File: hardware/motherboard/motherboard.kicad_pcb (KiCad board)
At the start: 2 copper layers, 220 x 150 mm, 14 parts, among them J1 01x02_Screw_ECG, J2 01x02_Screw_5VDC_IN, J3 RCA_L_Female_Tweeter, J4 RCA_R_Female_Sub, U1 DSP-MODULE_IDC_J3, U2 MCU-MODULE, U3 ECG-MODULE, U4 DSP-MODULE_IDC_J4, U5 PROTO-MODULE, U6 DSP-MODULE_RCA_J3

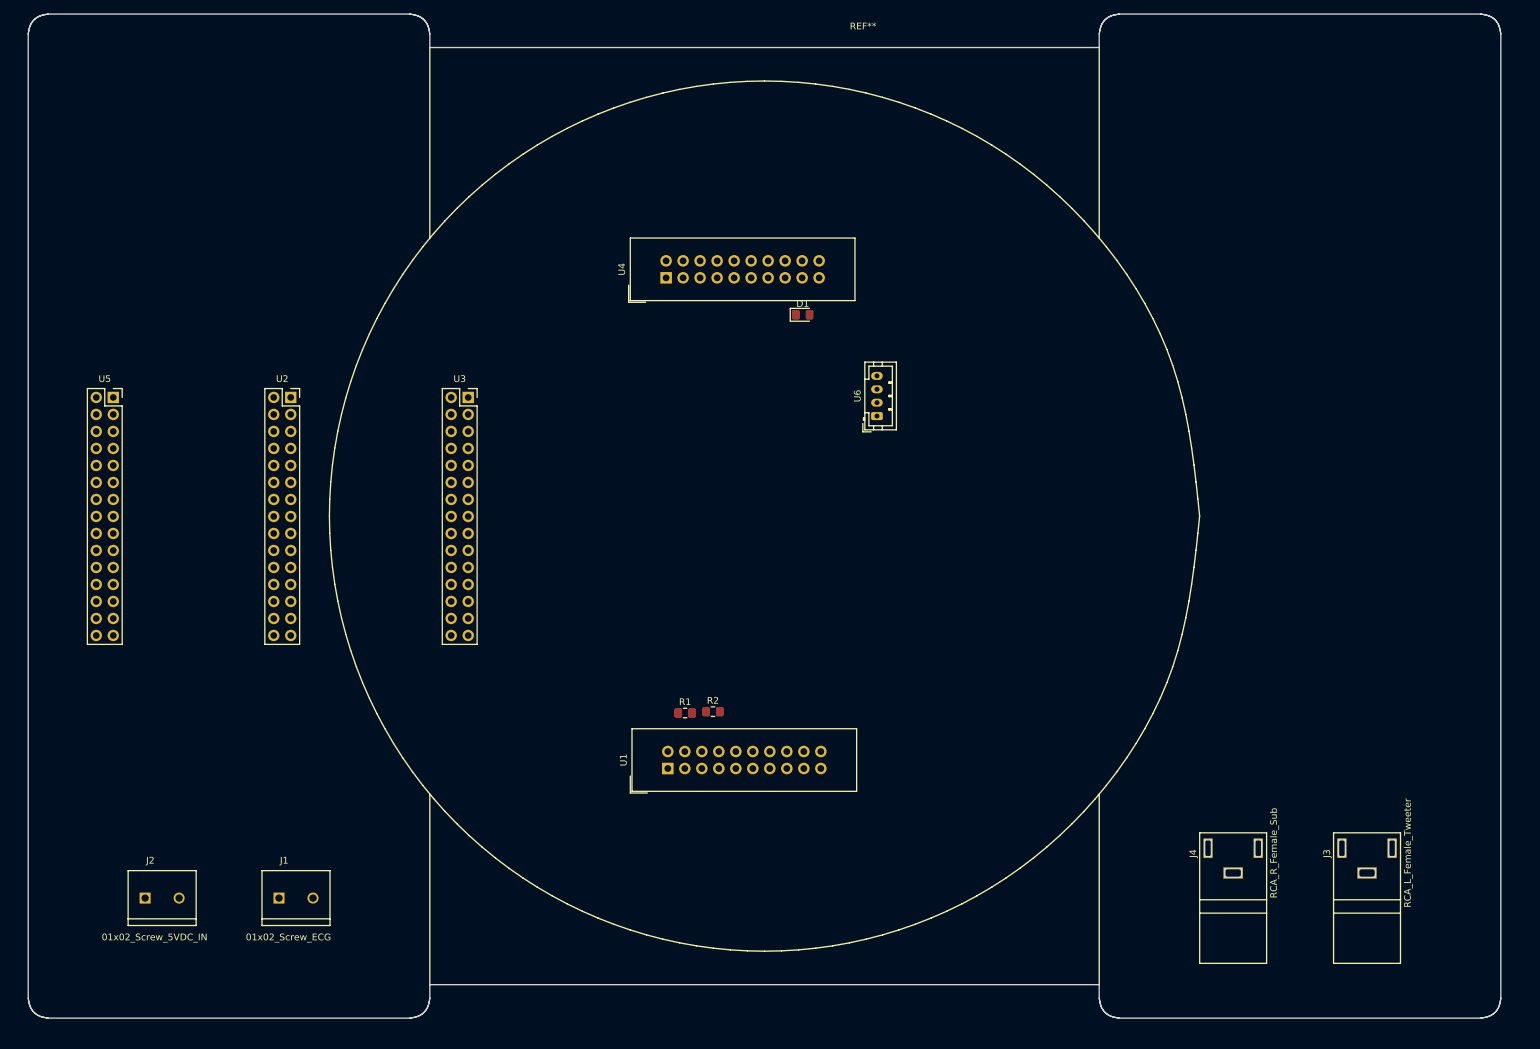
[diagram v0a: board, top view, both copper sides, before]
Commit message: [hw] Add jumper, pwr led, silkscreen logo to Motherboard
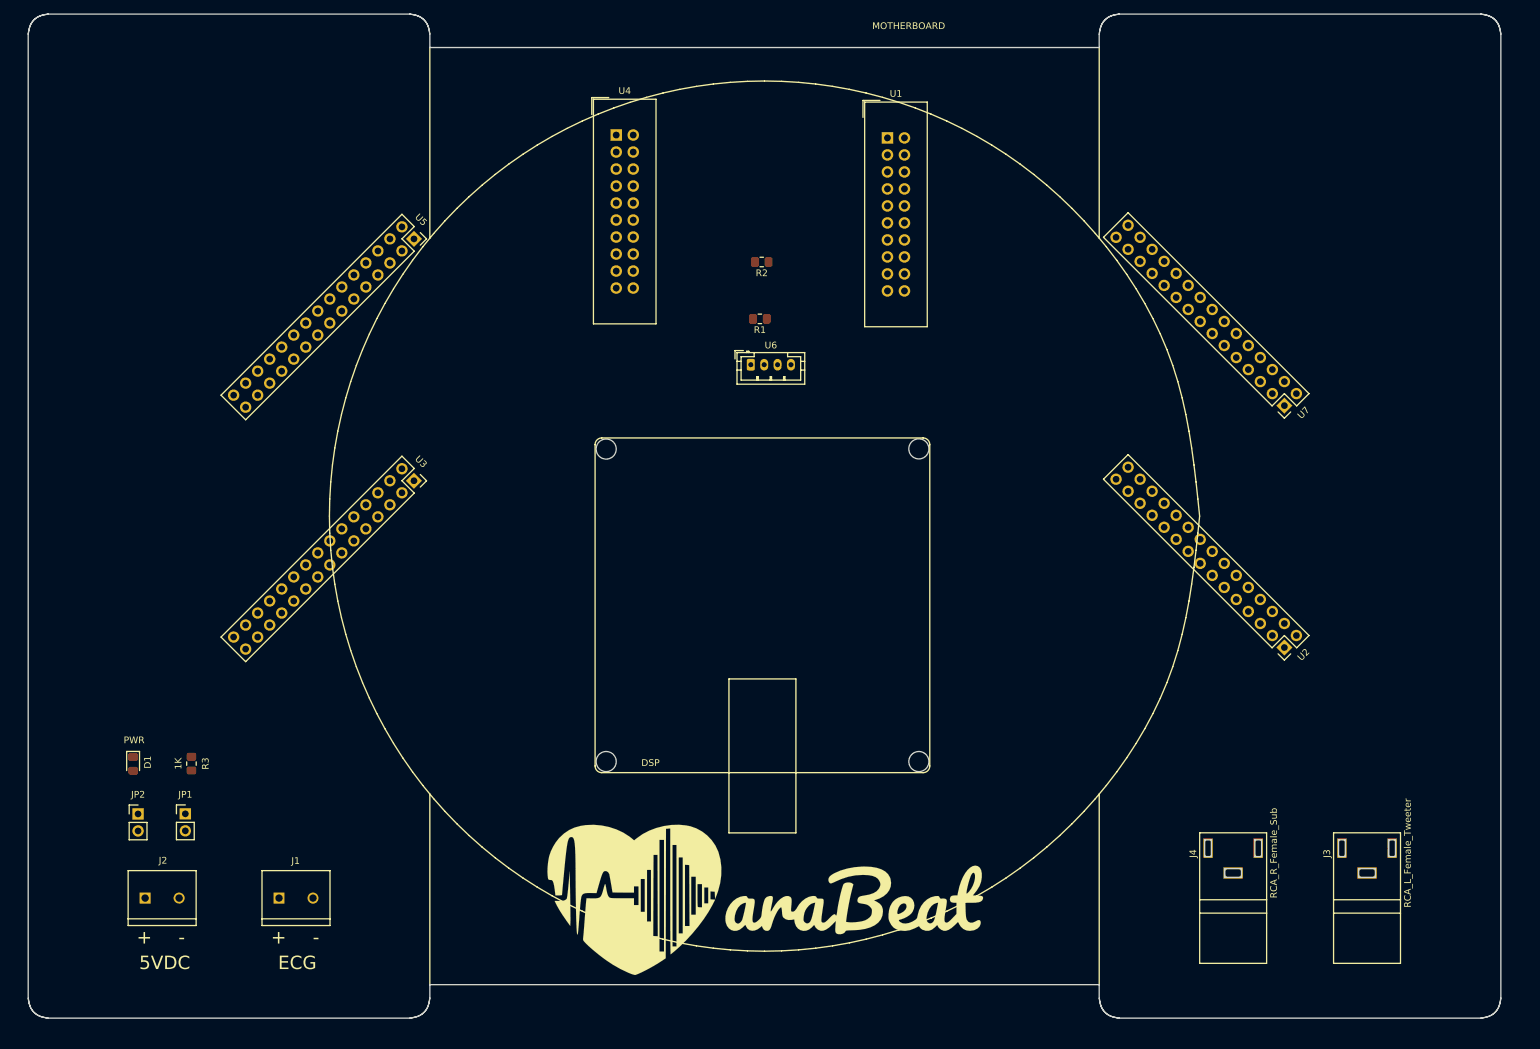
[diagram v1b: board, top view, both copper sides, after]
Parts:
- added DSP: WONDOM-DSP, ARABEAT:WONDOM-DSP, F.Cu at (129.7, 103.3)
- added G***: LOGO, ARABEAT:MOTHERBOARD-LOGO, F.Cu at (130.0, 147.3)
- added JP1: GND_Jumper, TE-CONNECTIVITY:382811-8, F.Cu at (43.5, 134.5)
- added JP2: 5V_Jumper, TE-CONNECTIVITY:382811-8, F.Cu at (36.4, 134.5)
- added R3: 1K, Resistor_SMD:R_0805_2012Metric_Pad1.15x1.40mm_HandSolder, F.Cu at (44.4, 126.9)
- added U7: PROTO-MODULE, Connector_PinSocket_2.54mm:PinSocket_2x15_P2.54mm_Vertical, F.Cu at (207.7, 73.5)
- moved U2 153.1 mm to (207.7, 109.6), turned to 225 degrees
- moved D1 120.4 mm to (35.7, 127.0), turned to 270 degrees
- moved U1 99.8 mm to (148.4, 33.5), turned to 0 degrees
- moved R2 67.6 mm to (129.6, 52.0), turned to 180 degrees
- moved R1 59.9 mm to (129.3, 60.5), turned to 180 degrees
- moved U5 50.8 mm to (77.6, 48.6), turned to 315 degrees
- moved U4 22.6 mm to (107.8, 33.1), turned to 0 degrees
- moved U6 20.3 mm to (127.9, 67.4), turned to 0 degrees
- moved U3 14.9 mm to (77.6, 84.7), turned to 315 degrees
- renumbered REF** to MOTHERBOARD
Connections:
- D1 pad 1: GND -> Net-(D1-Pad1)
- J2 pad 1: 5V -> Net-(J2-Pad1)
- J2 pad 2: GND -> Net-(J2-Pad2)
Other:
- board text added: "+"
- board text added: "-"
- board text added: "5VDC"
- board text added: "ECG"
- board text added: "PWR"

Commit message: [hw] Add mounting hole to mother board to fit into heated enclosure
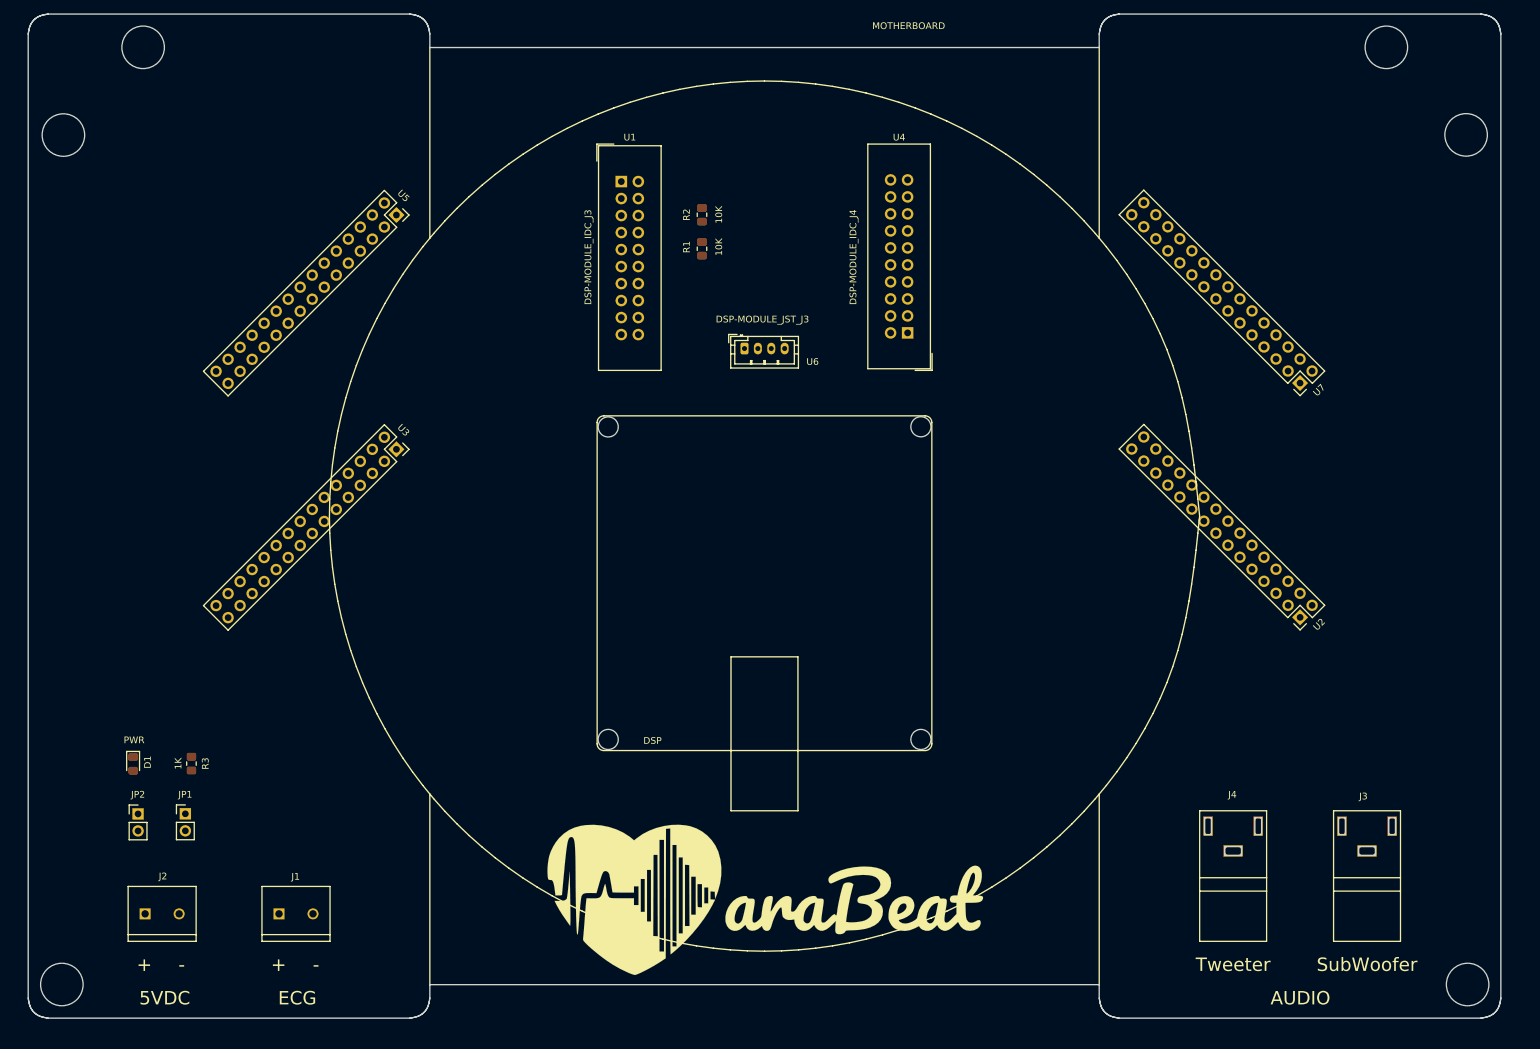
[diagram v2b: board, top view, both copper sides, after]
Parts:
- U6: value DSP-MODULE_RCA_J3 -> DSP-MODULE_JST_J3
- moved U4 52.6 mm to (151.4, 62.6), turned to 180 degrees
- moved U1 40.3 mm to (108.6, 40.0)
- moved R1 13.6 mm to (120.7, 50.0), turned to 90 degrees
- moved R2 11.4 mm to (120.7, 45.0), turned to 90 degrees
- moved U3 5.38 mm to (75.0, 80.0)
- moved U2 5.08 mm to (210.0, 105.1)
- moved U5 4.42 mm to (75.0, 45.0)
- moved U7 4.11 mm to (210.0, 70.1)
- moved DSP 3.32 mm to (130.0, 100.0)
- moved J3 3.29 mm to (220.0, 140.0)
- moved J4 3.29 mm to (200.0, 140.0)
- moved U6 2.59 mm to (127.0, 64.9)
- moved J1 2.36 mm to (60.0, 149.4)
- moved J2 2.36 mm to (40.0, 149.4)
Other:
- board text added: "AUDIO"
- board text added: "SubWoofer"
- board text added: "Tweeter"

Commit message: [hw] Route motherboard
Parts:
- added TP1: SCL, TestPoint:TestPoint_Keystone_5000-5004_Miniature, F.Cu at (54.9, 127.9)
- added TP2: SDA, TestPoint:TestPoint_Keystone_5000-5004_Miniature, F.Cu at (59.9, 127.9)
- added TP3: MISO, TestPoint:TestPoint_Keystone_5000-5004_Miniature, F.Cu at (64.9, 119.5)
- added TP4: MOSI, TestPoint:TestPoint_Keystone_5000-5004_Miniature, F.Cu at (59.9, 119.5)
- added TP5: SCK, TestPoint:TestPoint_Keystone_5000-5004_Miniature, F.Cu at (54.9, 119.5)
- added TP6: 5V, TestPoint:TestPoint_Keystone_5000-5004_Miniature, F.Cu at (59.9, 136.6)
- added TP7: 3V3, TestPoint:TestPoint_Keystone_5000-5004_Miniature, F.Cu at (54.9, 136.6)
- added TP8: GND, TestPoint:TestPoint_Keystone_5000-5004_Miniature, F.Cu at (64.9, 136.6)
- moved R2 9.40 mm to (130.0, 44.0)
- moved R1 9.35 mm to (130.0, 50.0)
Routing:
- net GND: track 0.00 -> 335.1 mm, vias 0 -> 1
- net 5V: track 0.00 -> 326.1 mm, vias 0 -> 3
- net 3V3: track 0.00 -> 290.9 mm, vias 0 -> 1
- net A4: track 0.00 -> 283.8 mm
- net A5: track 0.00 -> 274.9 mm, vias 0 -> 2
- net D12: track 0.00 -> 249.4 mm
- net D11: track 0.00 -> 246.0 mm
- net D13: track 0.00 -> 237.3 mm
- net D2: track 0.00 -> 223.6 mm
- net D8: track 0.00 -> 213.5 mm, vias 0 -> 1
- net D7: track 0.00 -> 211.6 mm, vias 0 -> 1
- net D3: track 0.00 -> 208.8 mm, vias 0 -> 1
- net D6: track 0.00 -> 201.2 mm, vias 0 -> 1
- net AREF: track 0.00 -> 201.2 mm
- net D1: track 0.00 -> 201.1 mm
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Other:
- net class PWR added: clearance 0.508, trace_width 0.508, via_dia 0.6, via_drill 0.3
- net class SIGNAL added: clearance 0.254, trace_width 0.254, via_dia 0.6, via_drill 0.3
- rule trace_min: 0.2 -> 0.1524
- rule via_min_size: 0.4 -> 0.6

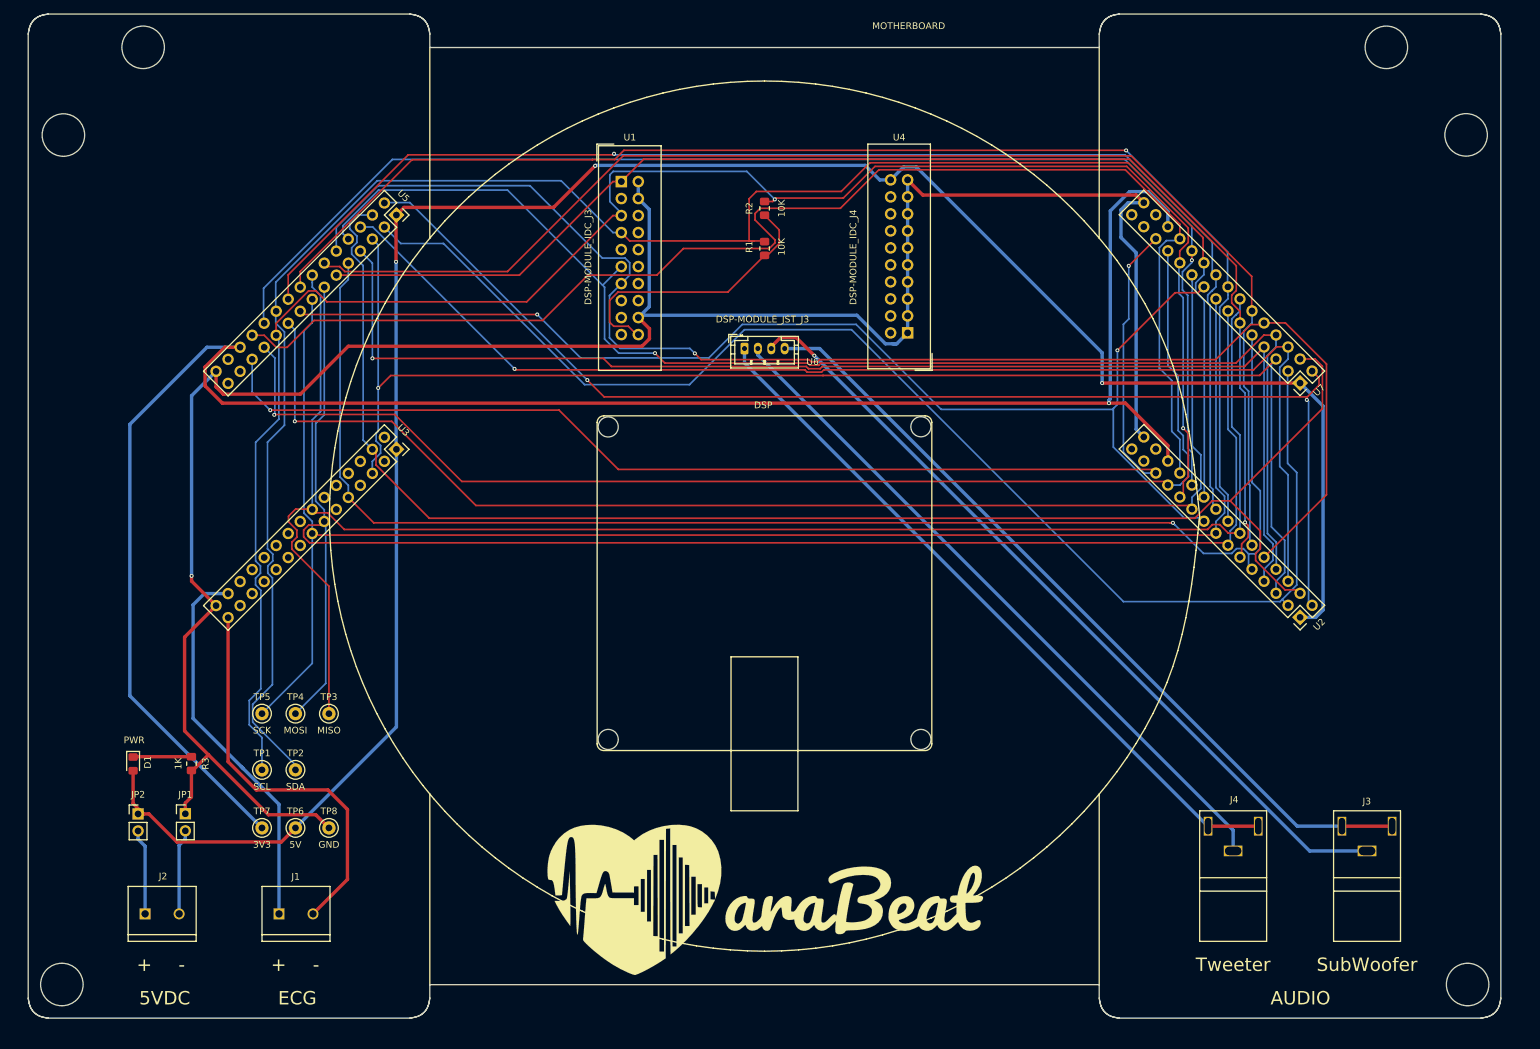
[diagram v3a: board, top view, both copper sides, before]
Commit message: [hw] Clean up traces on motherboard
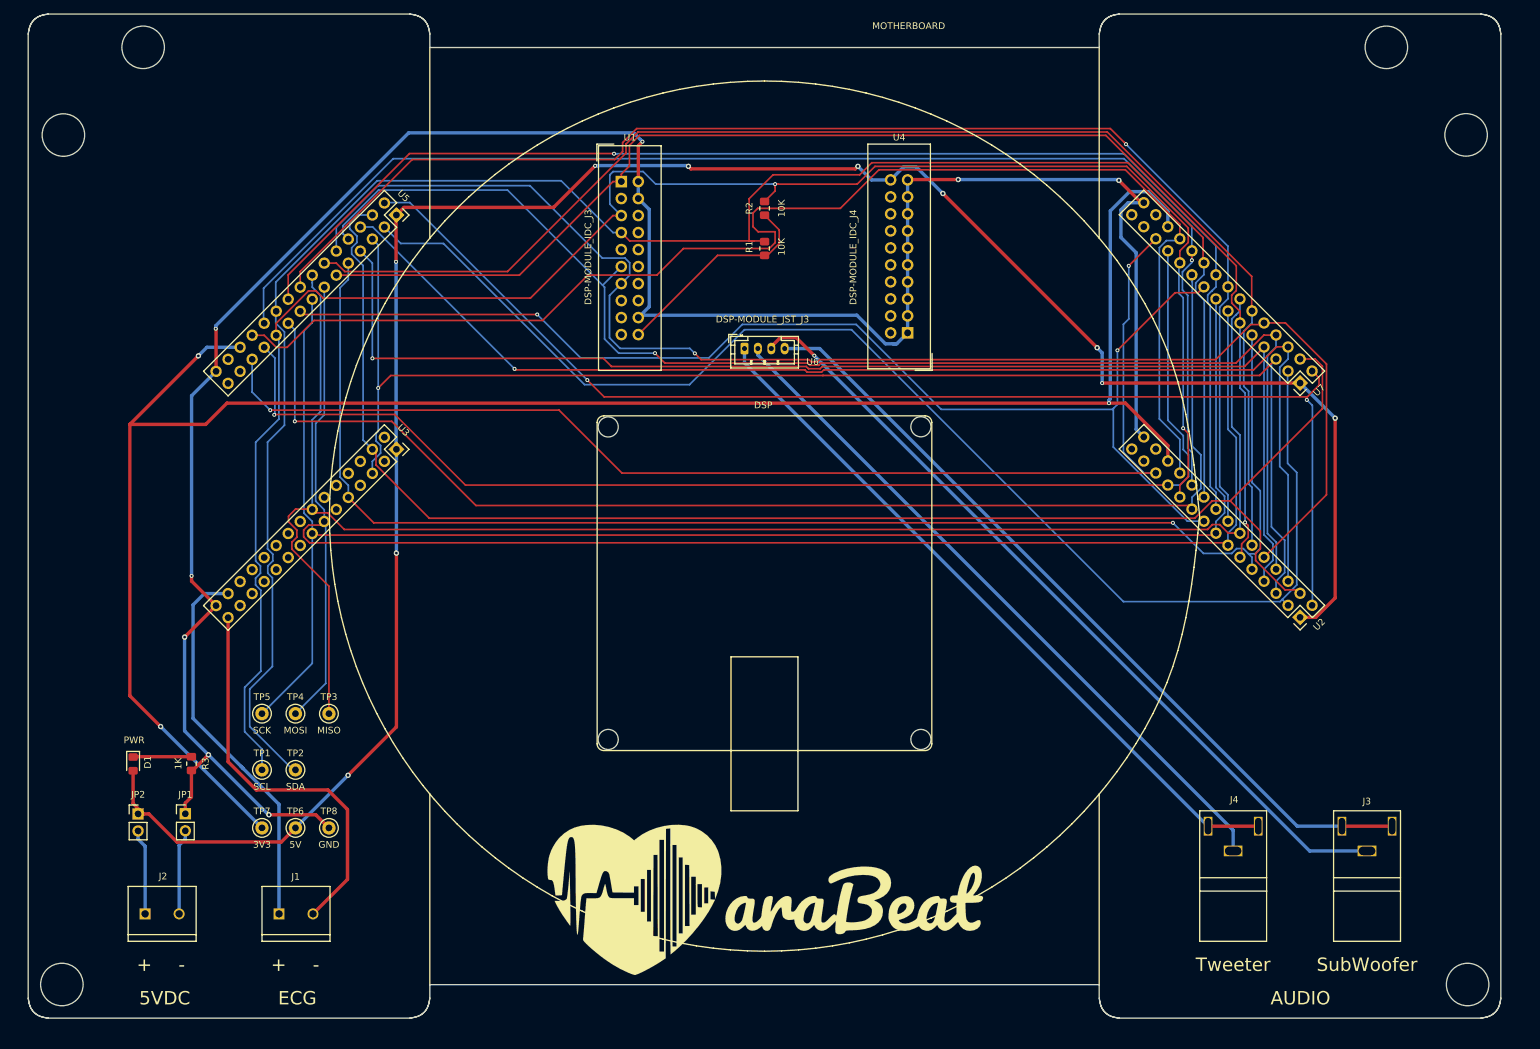
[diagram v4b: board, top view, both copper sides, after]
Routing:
- net GND: track 335.1 -> 349.7 mm, vias 1 -> 8
- net Net-(R1-Pad1): track 42.3 -> 32.1 mm
- net D9: track 193.6 -> 199.0 mm
- net A0: track 195.9 -> 199.9 mm
- net D10: track 194.9 -> 198.6 mm
- net 3V3: track 290.9 -> 293.1 mm, vias 1 -> 3
- net AREF: track 201.2 -> 203.2 mm
- net 5V: track 326.1 -> 327.6 mm, vias 3 -> 10
- net A4: track 283.8 -> 284.4 mm
